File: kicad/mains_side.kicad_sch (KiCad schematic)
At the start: 40 parts, among them P1 Conn_WallPlug, Q1 Q_Photo_NPN

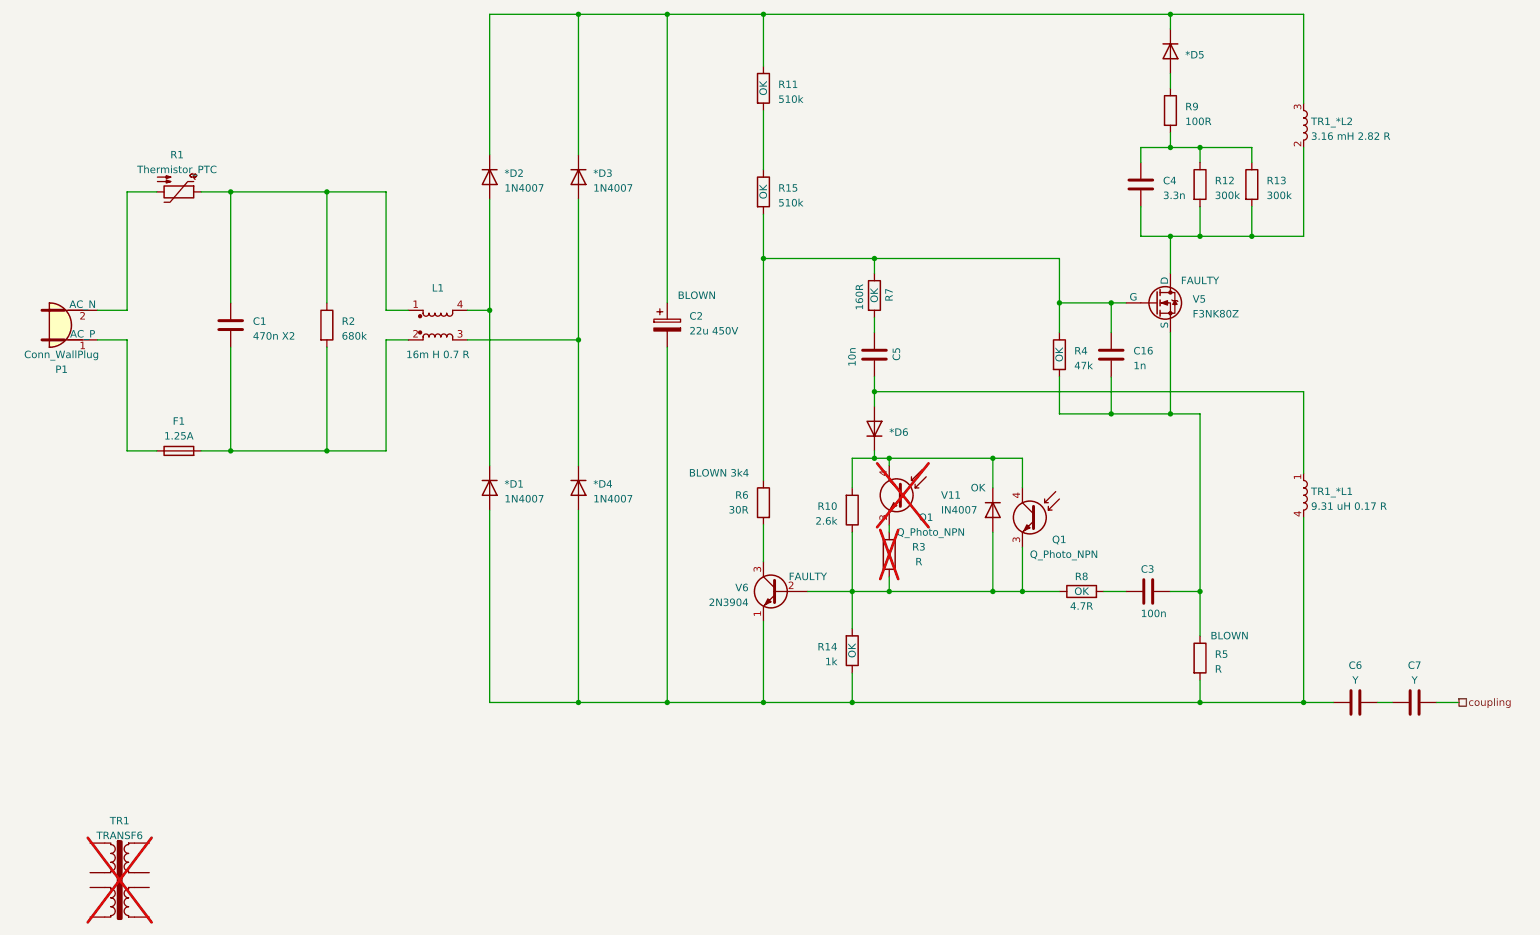
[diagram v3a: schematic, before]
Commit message: Repair resonant circuitry
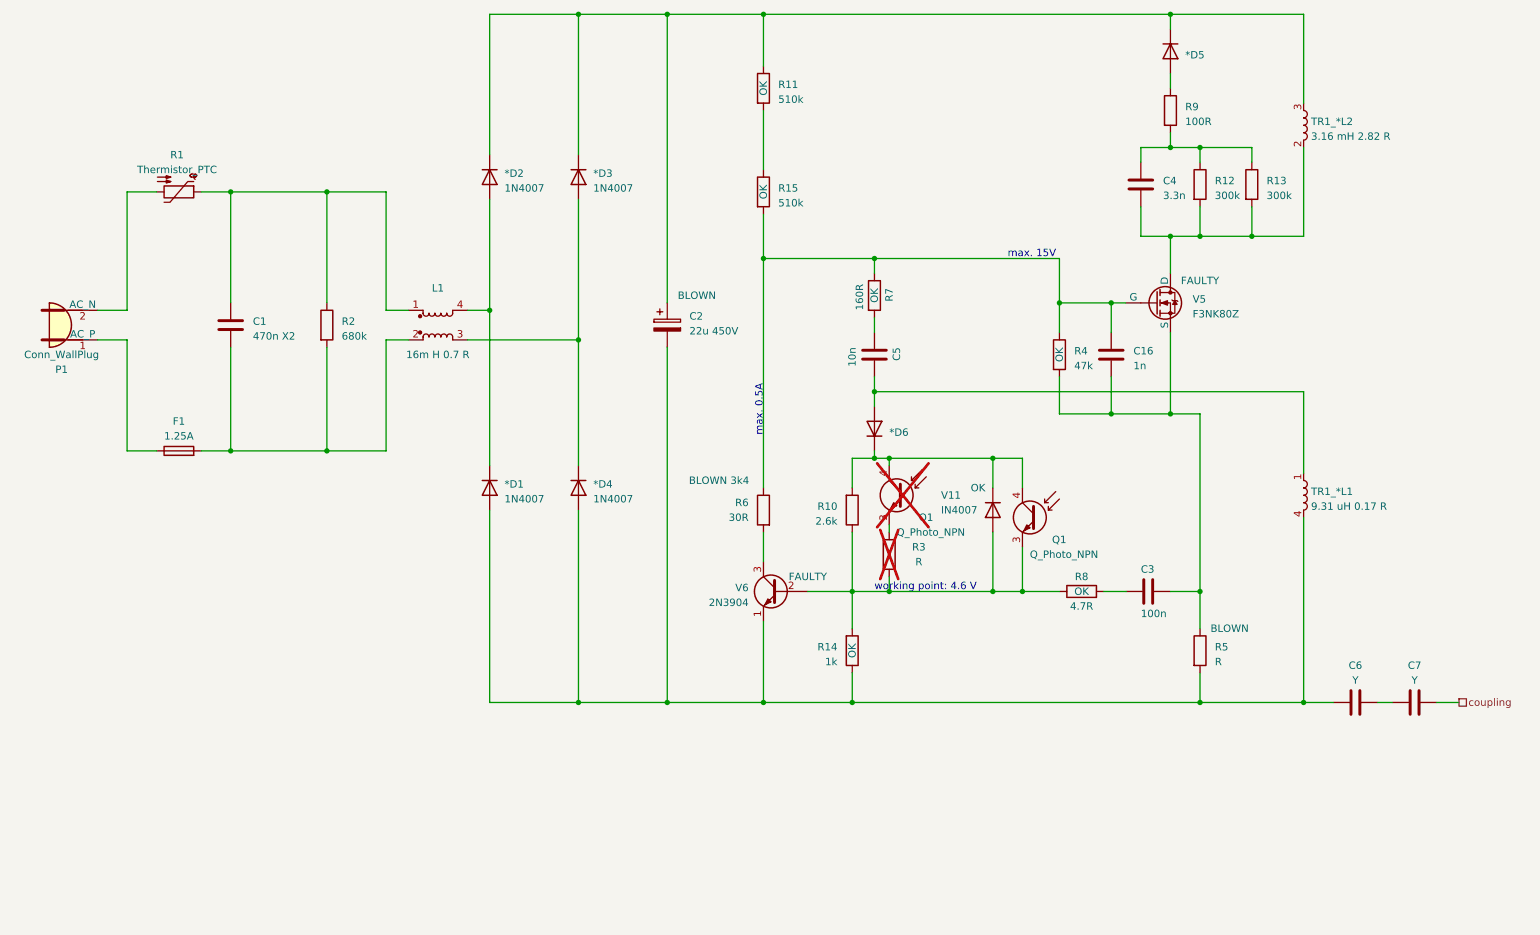
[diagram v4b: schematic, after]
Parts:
- removed TR1: TRANSF6, symbol Transformer:TRANSF6
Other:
- note added: "max. 0.5A"
- note added: "max. 15V"
- note added: "working point: 4.6 V"
- moved on the sheet: R5, R6
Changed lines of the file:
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@@
     (stroke (width 0) (type default))
   )
-  (wire (pts (xy 148.59 73.66) (xy 148.59 111.76))
+  (wire (pts (xy 148.59 73.66) (xy 148.59 113.03))
     (stroke (width 0) (type default))
   )
@@
     (stroke (width 0) (type default))
   )
-  (wire (pts (xy 223.52 146.05) (xy 223.52 149.86))
+  (wire (pts (xy 223.52 144.78) (xy 223.52 149.86))
     (stroke (width 0) (type default))
   )
@@
     (stroke (width 0) (type default))
   )
-  (wire (pts (xy 148.59 119.38) (xy 148.59 125.73))
+  (wire (pts (xy 148.59 120.65) (xy 148.59 125.73))
     (stroke (width 0) (type default))
   )
@@
     (stroke (width 0) (type default))
   )
-  (wire (pts (xy 223.52 130.81) (xy 223.52 138.43))
+  (wire (pts (xy 223.52 130.81) (xy 223.52 137.16))
     (stroke (width 0) (type default))
   )
@@
   (wire (pts (xy 83.82 82.55) (xy 87.63 82.55))
     (stroke (width 0) (type default))
+  )
+  (text "max. 15V" (at 190.5 73.66 0)
+    (effects (font (size 1.27 1.27)) (justify left bottom))
+  )
+  (text "max. 0.5A" (at 148.59 104.14 90)
+    (effects (font (size 1.27 1.27)) (justify left bottom))
+  )
+  (text "working point: 4.6 V" (at 167.64 130.81 0)
+    (effects (font (size 1.27 1.27)) (justify left bottom))
   )
   (hierarchical_label "coupling" (shape passive) (at 267.97 149.86 0) (fields_autoplaced)
@@
     )
   )
-  (symbol (lib_id "Device:R") (at 148.59 115.57 0) (mirror y) (unit 1)
+  (symbol (lib_id "Device:R") (at 148.59 116.84 0) (mirror y) (unit 1)
     (in_bom yes) (on_board yes) (dnp no)
-    (property "Reference" "R6" (at 146.05 114.3 0)
-      (effects (font (size 1.27 1.27)) (justify left))
-    )
-    (property "Value" "30R" (at 146.05 116.84 0)
-      (effects (font (size 1.27 1.27)) (justify left))
-    )
-    (property "Footprint" "Resistor_THT:R_Axial_DIN0207_L6.3mm_D2.5mm_P10.16mm_Horizontal" (at 150.368 115.57 90)
-      (effects (font (size 1.27 1.27)) hide)
-    )
-    (property "Datasheet" "~" (at 148.59 115.57 0)
-      (effects (font (size 1.27 1.27)) hide)
-    )
-    (property "Tested" "BLOWN 3k4" (at 140.97 110.49 0)
+    (property "Reference" "R6" (at 146.05 115.57 0)
+      (effects (font (size 1.27 1.27)) (justify left))
+    )
+    (property "Value" "30R" (at 146.05 118.11 0)
+      (effects (font (size 1.27 1.27)) (justify left))
+    )
+    (property "Footprint" "Resistor_THT:R_Axial_DIN0207_L6.3mm_D2.5mm_P10.16mm_Horizontal" (at 150.368 116.84 90)
+      (effects (font (size 1.27 1.27)) hide)
+    )
+    (property "Datasheet" "~" (at 148.59 116.84 0)
+      (effects (font (size 1.27 1.27)) hide)
+    )
+    (property "Tested" "BLOWN 3k4" (at 140.97 111.76 0)
       (effects (font (size 1.27 1.27)))
     )
@@
     )
   )
-  (symbol (lib_id "Transformer:TRANSF6") (at 38.1 181.61 0) (unit 1)
-    (in_bom no) (on_board no) (dnp yes) (fields_autoplaced)
-    (property "Reference" "TR1" (at 38.1 170.18 0)
-      (effects (font (size 1.27 1.27)))
-    )
-    (property "Value" "TRANSF6" (at 38.1 172.72 0)
-      (effects (font (size 1.27 1.27)))
-    )
-    (property "Footprint" "" (at 38.1 181.61 0)
-      (effects (font (size 1.27 1.27)) hide)
-    )
-    (property "Datasheet" "" (at 38.1 181.61 0)
-      (effects (font (size 1.27 1.27)) hide)
-    )
-    (property "Sim.Enable" "0" (at 38.1 181.61 0)
-      (effects (font (size 1.27 1.27)) hide)
-    )
-    (pin "1")
-    (pin "2")
-    (pin "3")
-    (pin "4")
-    (pin "5")
-    (pin "6")
-    (pin "7")
-    (pin "8")
-    (instances
-      (project "Dremel_PCB1857_V1"
-        (path "/ab18b4c8-6f40-44db-bccd-b69c22b3ada9/a48cdbeb-6ee2-4275-8de1-cf332eca272a"
-          (reference "TR1") (unit 1)
-        )
-        (path "/ab18b4c8-6f40-44db-bccd-b69c22b3ada9/4c8f6a8b-06f4-4e61-8fed-29a27b18ce1c"
-          (reference "TR1") (unit 1)
-        )
-      )
-    )
-  )
   (symbol (lib_id "Device:C") (at 213.36 60.96 0) (unit 1)
     (in_bom yes) (on_board yes) (dnp no) (fields_autoplaced)
@@
     )
   )
-  (symbol (lib_id "Device:R") (at 223.52 142.24 0) (unit 1)
+  (symbol (lib_id "Device:R") (at 223.52 140.97 0) (unit 1)
     (in_bom yes) (on_board yes) (dnp no)
-    (property "Reference" "R5" (at 226.06 141.605 0)
-      (effects (font (size 1.27 1.27)) (justify left))
-    )
-    (property "Value" "R" (at 226.06 144.145 0)
-      (effects (font (size 1.27 1.27)) (justify left))
-    )
-    (property "Footprint" "Resistor_THT:R_Axial_DIN0207_L6.3mm_D2.5mm_P10.16mm_Horizontal" (at 221.742 142.24 90)
-      (effects (font (size 1.27 1.27)) hide)
-    )
-    (property "Datasheet" "~" (at 223.52 142.24 0)
-      (effects (font (size 1.27 1.27)) hide)
-    )
-    (property "Tested" "BLOWN" (at 228.6 138.43 0)
+    (property "Reference" "R5" (at 226.06 140.335 0)
+      (effects (font (size 1.27 1.27)) (justify left))
+    )
+    (property "Value" "R" (at 226.06 142.875 0)
+      (effects (font (size 1.27 1.27)) (justify left))
+    )
+    (property "Footprint" "Resistor_THT:R_Axial_DIN0207_L6.3mm_D2.5mm_P10.16mm_Horizontal" (at 221.742 140.97 90)
+      (effects (font (size 1.27 1.27)) hide)
+    )
+    (property "Datasheet" "~" (at 223.52 140.97 0)
+      (effects (font (size 1.27 1.27)) hide)
+    )
+    (property "Tested" "BLOWN" (at 228.6 137.16 0)
       (effects (font (size 1.27 1.27)))
     )
@@
       (effects (font (size 1.27 1.27)) hide)
     )
-    (property "Datasheet" "https://ngspice.sourceforge.io/docs/ngspice-manual.pdf" (at 215.9 93.98 0)
-      (effects (font (size 1.27 1.27)) hide)
-    )
+    (property "Datasheet" "https://4donline.ihs.com/images/VipMasterIC/IC/SGST/SGST-S-A0003061510/SGST-S-A0003061510-1.pdf?hkey=6D3A4C79FDBF58556ACFDE234799DDF0" (at 215.9 93.98 0)
+      (effects (font (size 1.27 1.27)) hide)
+    )

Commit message: Plugged in battery -> firework
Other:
- note added: "Abs. max. Vbe = 6V"
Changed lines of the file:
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@@
+    (effects (font (size 1.27 1.27)) (justify left bottom))
+  )
+  (text "Abs. max. Vbe = 6V" (at 140.97 138.43 0)
     (effects (font (size 1.27 1.27)) (justify left bottom))
   )

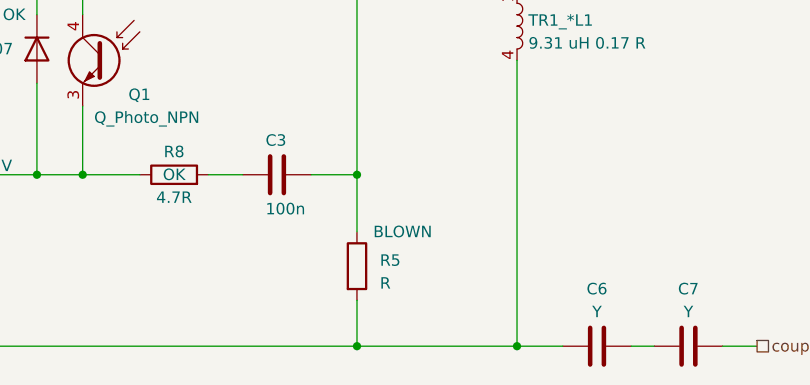
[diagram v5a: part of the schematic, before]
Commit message: Add R5 value
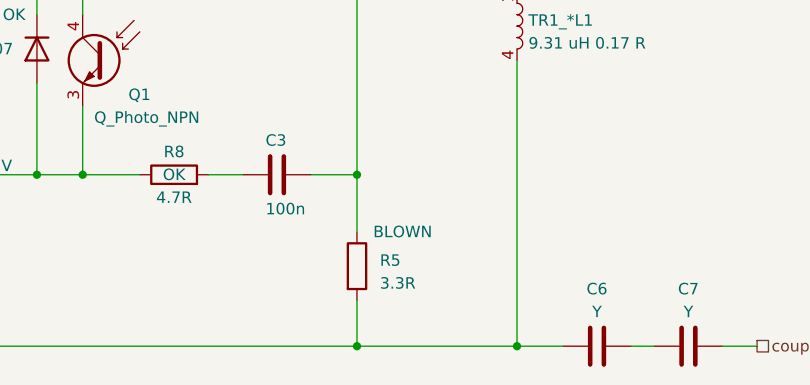
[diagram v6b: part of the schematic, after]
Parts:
- R5: value R -> 3.3R
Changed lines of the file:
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@@
       (effects (font (size 1.27 1.27)) (justify left))
     )
-    (property "Value" "R" (at 226.06 142.875 0)
+    (property "Value" "3.3R" (at 226.06 142.875 0)
       (effects (font (size 1.27 1.27)) (justify left))
     )
